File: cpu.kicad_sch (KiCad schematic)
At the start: 30 parts, among them J81 Conn_01x03_Pin, J82 Conn_Coaxial, J83 Conn_Coaxial, J84 Conn_01x02_Pin, SW81 SW_Push, SW82 SW_Push, U8 ESP32-C6-MINI-1U, U81 74HC595, U82 74HC595, U83 74HC595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

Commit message: Scan deleted.
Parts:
- removed C90: 0u1, Capacitor_SMD:C_0402_1005Metric, symbol Device:C
- removed U83: 74HC595, Package_SO:SOIC-16_3.9x9.9mm_P1.27mm, symbol 74xx:74HC595
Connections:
- net MonA0: now also U82.3 (QD)
- net MonA1: now also U82.2 (QC)
- net MonB0: now also U82.1 (QB)
- net MonB1: now also U82.15 (QA)
- net OffsetA0: no longer U82.7 (QH)
- net OffsetA1: no longer U82.6 (QG)
- net OffsetA2: no longer U82.5 (QF)
- net SHSel: no longer U82.4 (QE)
- net Sel1A: now also U82.7 (QH)
- net Sel1B: now also U82.6 (QG)
- net Sel2A: now also U82.5 (QF)
- net Sel2B: now also U82.4 (QE)
- net SHHoldG1: no longer names the net of U81.4 (QE)
- net SHHoldG2: no longer names the net of U81.15 (QA)
- net SHOutEn1: no longer names the net of U81.7 (QH)
- net SHOutEn2: no longer names the net of U81.3 (QD)
- net SHSample1: no longer names the net of U81.6 (QG)
- net SHSample2: no longer names the net of U81.2 (QC)
- net SHSampleG1: no longer names the net of U81.5 (QF)
- net SHSampleG2: no longer names the net of U81.1 (QB)
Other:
- moved on the sheet: C87, C88, C89, R87, U81, U82

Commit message: Most blocks there....
About to restore scan.
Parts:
- R83: footprint Resistor_SMD:R_0603_1608Metric -> Resistor_SMD:R_0402_1005Metric; LCSC C23140 -> C25105
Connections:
- net OffsetA0: now also U81.7 (QH)
- net OffsetA1: now also U81.6 (QG)
- net OffsetA2: now also U81.5 (QF)
- net SHSel: now also U81.4 (QE)
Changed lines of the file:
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@@
 	)
 	(no_connect
-		(at 119.38 107.95)
+		(at 118.11 107.95)
 	)
 	(no_connect
@@
 	)
 	(no_connect
-		(at 119.38 113.03)
+		(at 118.11 113.03)
 	)
 	(no_connect
@@
 	)
 	(no_connect
-		(at 119.38 105.41)
+		(at 118.11 105.41)
 	)
 	(no_connect
@@
 	)
 	(no_connect
-		(at 119.38 110.49)
+		(at 118.11 110.49)
 	)
 	(no_connect
@@
 	(wire
 		(pts
-			(xy 119.38 123.19) (xy 120.65 123.19)
-		)
-		(stroke
-			(width 0)
-			(type default)
-		)
-	)
-	(wire
-		(pts
-			(xy 119.38 118.11) (xy 120.65 118.11)
-		)
-		(stroke
-			(width 0)
-			(type default)
-		)
-	)
-	(wire
-		(pts
 			(xy 170.18 115.57) (xy 171.45 115.57)
 		)
@@
 	(wire
 		(pts
-			(xy 119.38 115.57) (xy 120.65 115.57)
-		)
-		(stroke
-			(width 0)
-			(type default)
-		)
-	)
-	(wire
-		(pts
 			(xy 57.15 48.26) (xy 80.01 48.26)
 		)
@@
 	(wire
 		(pts
-			(xy 119.38 120.65) (xy 120.65 120.65)
-		)
-		(stroke
-			(width 0)
-			(type default)
-		)
-	)
-	(wire
-		(pts
 			(xy 71.12 71.12) (xy 80.01 71.12)
 		)
@@
 	(hierarchical_label "OffsetA0"
 		(shape output)
-		(at 120.65 123.19 0)
+		(at 118.11 123.19 0)
 		(effects
 			(font
@@
 	(hierarchical_label "SHSel"
 		(shape output)
-		(at 120.65 115.57 0)
+		(at 118.11 115.57 0)
 		(effects
 			(font
@@
 	(hierarchical_label "OffsetA2"
 		(shape output)
-		(at 120.65 118.11 0)
+		(at 118.11 118.11 0)
 		(effects
 			(font
@@
 	(hierarchical_label "OffsetA1"
 		(shape output)
-		(at 120.65 120.65 0)
+		(at 118.11 120.65 0)
 		(effects
 			(font
@@
 	)
 	(symbol
-		(lib_name "Conn_Coaxial_1")
 		(lib_id "Connector:Conn_Coaxial")
 		(at 190.5 62.23 0)
@@
 			)
 		)
-		(property "Footprint" "Resistor_SMD:R_0603_1608Metric"
+		(property "Footprint" "Resistor_SMD:R_0402_1005Metric"
 			(at 175.26 60.452 90)
 			(effects
@@
 			)
 		)
-		(property "LCSC" "C23140"
+		(property "LCSC" "C25105"
 			(at 175.26 62.23 90)
 			(effects

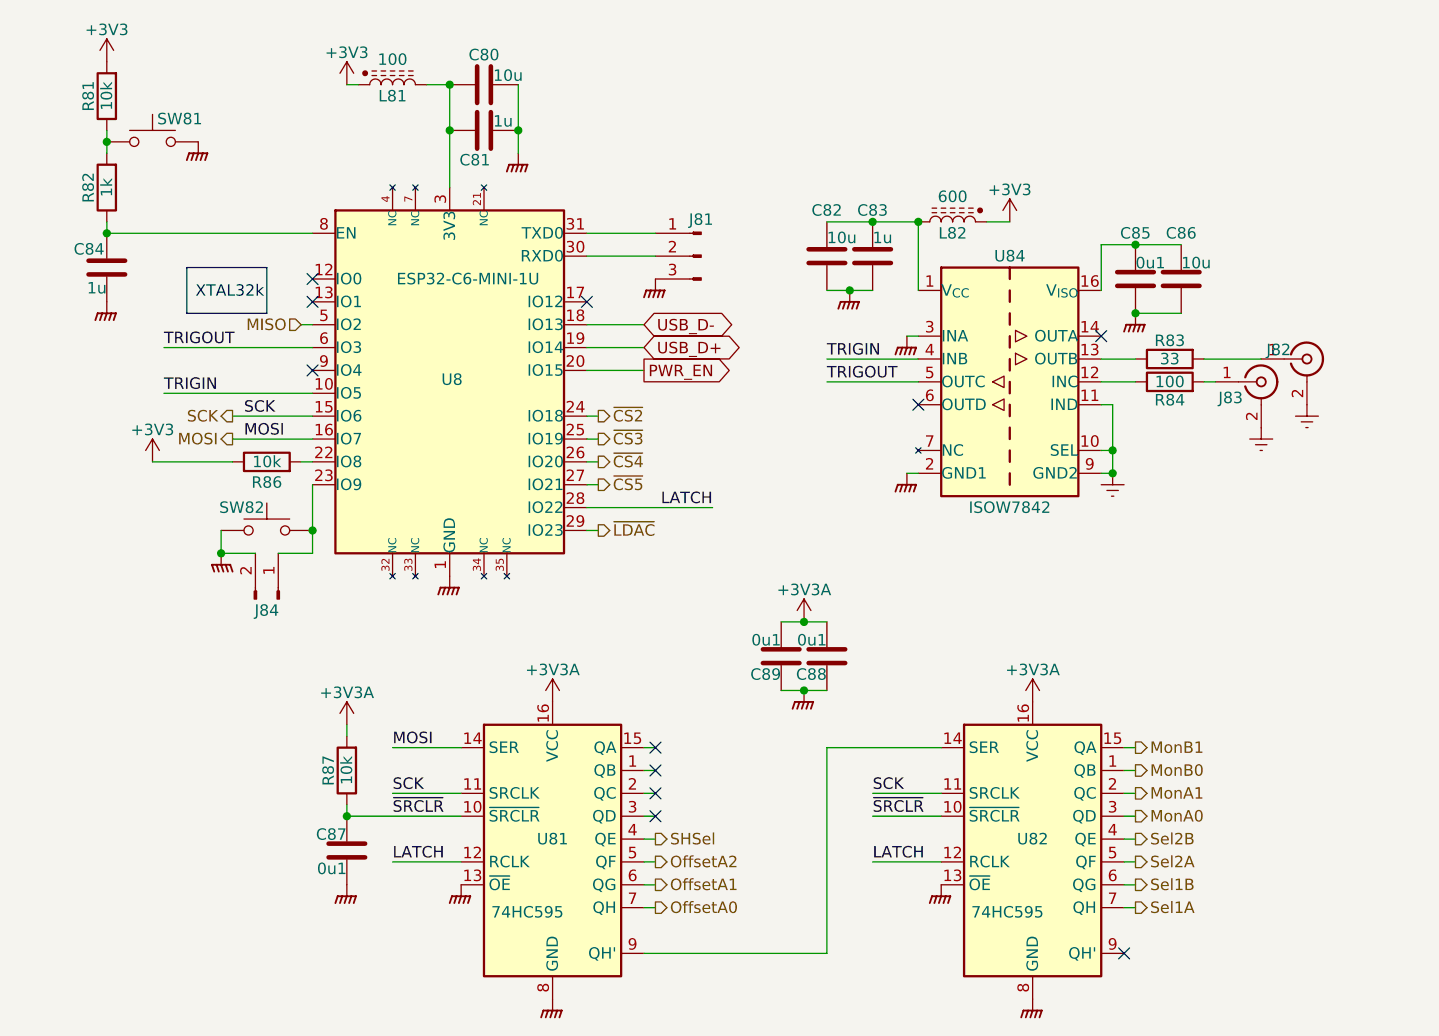
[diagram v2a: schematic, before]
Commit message: Put ref filtering into the schematic.
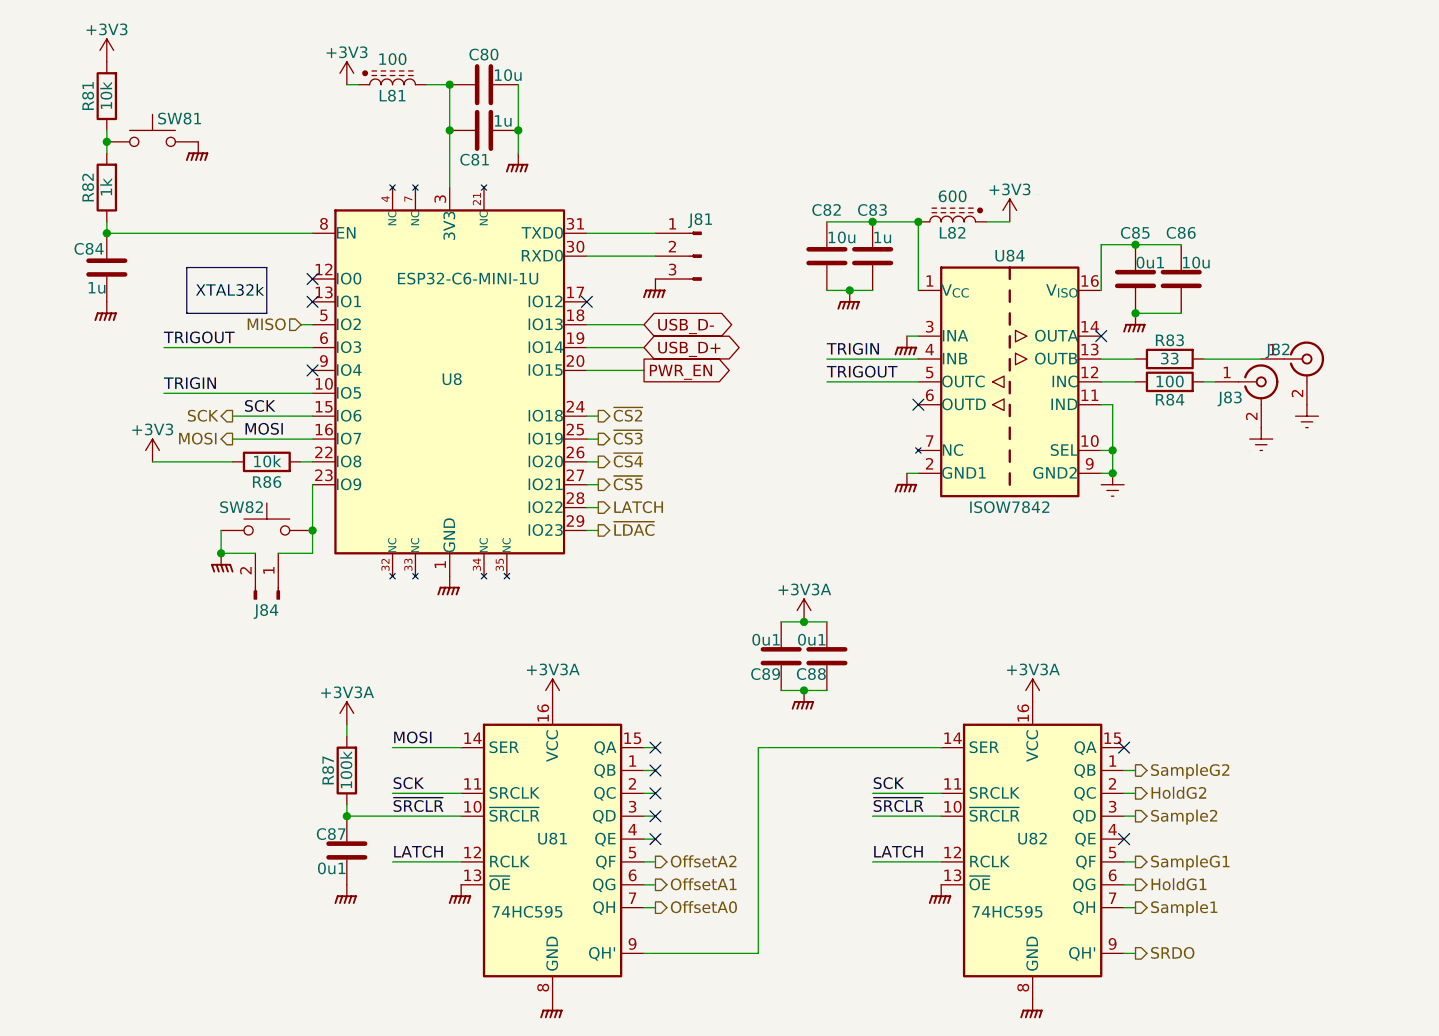
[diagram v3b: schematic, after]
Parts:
- R87: value 10k -> 100k; LCSC C25744 -> (none)
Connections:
- net SRDO: now reaches U82.9 (QH')
- net MonA0 renamed Sample2
- net MonA1 renamed HoldG2
- net MonB0 renamed SampleG2
- net MonB1: no longer names the net of U82.15 (QA)
- net SHSel: no longer names the net of U81.4 (QE)
- net Sel1A renamed Sample1
- net Sel1B renamed HoldG1
- net Sel2A renamed SampleG1
- net Sel2B: no longer names the net of U82.4 (QE)
- no-connect marks 11 -> 13
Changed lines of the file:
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@@
 	)
 	(no_connect
+		(at 170.18 105.41)
+	)
+	(no_connect
+		(at 118.11 115.57)
+	)
+	(no_connect
 		(at 118.11 113.03)
 	)
 	(no_connect
-		(at 80.01 53.34)
+		(at 170.18 115.57)
 	)
 	(no_connect
-		(at 118.11 105.41)
+		(at 80.01 53.34)
 	)
 	(no_connect
-		(at 170.18 128.27)
+		(at 118.11 105.41)
 	)
 	(no_connect
@@
 	(wire
 		(pts
-			(xy 170.18 105.41) (xy 171.45 105.41)
+			(xy 76.2 83.82) (xy 80.01 83.82)
 		)
 		(stroke
@@
 	(wire
 		(pts
-			(xy 76.2 83.82) (xy 80.01 83.82)
+			(xy 129.54 105.41) (xy 149.86 105.41)
 		)
 		(stroke
@@
 	(wire
 		(pts
-			(xy 137.16 105.41) (xy 149.86 105.41)
+			(xy 146.05 59.69) (xy 147.32 59.69)
 		)
 		(stroke
@@
 	(wire
 		(pts
-			(xy 146.05 59.69) (xy 147.32 59.69)
+			(xy 170.18 113.03) (xy 171.45 113.03)
 		)
 		(stroke
@@
 	(wire
 		(pts
-			(xy 137.16 128.27) (xy 116.84 128.27)
+			(xy 129.54 128.27) (xy 116.84 128.27)
 		)
 		(stroke
@@
 	(wire
 		(pts
-			(xy 171.45 49.53) (xy 176.53 49.53)
+			(xy 170.18 107.95) (xy 171.45 107.95)
 		)
 		(stroke
@@
 	(wire
 		(pts
-			(xy 170.18 113.03) (xy 171.45 113.03)
+			(xy 170.18 110.49) (xy 171.45 110.49)
 		)
 		(stroke
@@
 	(wire
 		(pts
-			(xy 83.82 102.87) (xy 83.82 104.14)
+			(xy 171.45 49.53) (xy 176.53 49.53)
 		)
 		(stroke
@@
 	(wire
 		(pts
-			(xy 88.9 110.49) (xy 96.52 110.49)
+			(xy 83.82 102.87) (xy 83.82 104.14)
 		)
 		(stroke
@@
 	(wire
 		(pts
-			(xy 170.18 115.57) (xy 171.45 115.57)
+			(xy 88.9 110.49) (xy 96.52 110.49)
 		)
 		(stroke
@@
 	(wire
 		(pts
-			(xy 110.49 78.74) (xy 124.46 78.74)
+			(xy 110.49 78.74) (xy 111.76 78.74)
 		)
 		(stroke
@@
 	(wire
 		(pts
-			(xy 146.05 74.93) (xy 147.32 74.93)
+			(xy 170.18 128.27) (xy 171.45 128.27)
 		)
 		(stroke
@@
 	(wire
 		(pts
-			(xy 167.64 49.53) (xy 171.45 49.53)
+			(xy 146.05 74.93) (xy 147.32 74.93)
 		)
 		(stroke
@@
 	(wire
 		(pts
-			(xy 179.07 64.77) (xy 180.34 64.77)
+			(xy 167.64 49.53) (xy 171.45 49.53)
 		)
 		(stroke
@@
 	(wire
 		(pts
-			(xy 78.74 73.66) (xy 80.01 73.66)
+			(xy 179.07 64.77) (xy 180.34 64.77)
 		)
 		(stroke
@@
 	(wire
 		(pts
-			(xy 170.18 107.95) (xy 171.45 107.95)
+			(xy 78.74 73.66) (xy 80.01 73.66)
 		)
 		(stroke
@@
 	(wire
 		(pts
-			(xy 137.16 128.27) (xy 137.16 105.41)
+			(xy 129.54 128.27) (xy 129.54 105.41)
 		)
 		(stroke
@@
 	(wire
 		(pts
-			(xy 170.18 110.49) (xy 171.45 110.49)
-		)
-		(stroke
-			(width 0)
-			(type default)
-		)
-	)
-	(wire
-		(pts
 			(xy 83.82 111.76) (xy 83.82 113.03)
 		)
@@
 		)
 	)
-	(label "LATCH"
-		(at 124.46 78.74 180)
-		(effects
-			(font
-				(size 1.27 1.27)
-			)
-			(justify right bottom)
-		)
-	)
 	(label "SCK"
 		(at 72.39 68.58 0)
@@
 		)
 	)
-	(hierarchical_label "MonA1"
+	(hierarchical_label "HoldG2"
 		(shape output)
 		(at 171.45 110.49 0)
@@
 		)
 	)
-	(hierarchical_label "Sel2B"
+	(hierarchical_label "Sample2"
 		(shape output)
-		(at 171.45 115.57 0)
+		(at 171.45 113.03 0)
 		(effects
 			(font
@@
 		)
 	)
-	(hierarchical_label "Sel1B"
+	(hierarchical_label "SampleG1"
 		(shape output)
-		(at 171.45 120.65 0)
+		(at 171.45 118.11 0)
 		(effects
 			(font
@@
 		)
 	)
-	(hierarchical_label "SHSel"
+	(hierarchical_label "~{LDAC}"
 		(shape output)
-		(at 118.11 115.57 0)
+		(at 111.76 81.28 0)
 		(effects
 			(font
@@
 		)
 	)
-	(hierarchical_label "~{LDAC}"
+	(hierarchical_label "OffsetA2"
 		(shape output)
-		(at 111.76 81.28 0)
+		(at 118.11 118.11 0)
 		(effects
 			(font
@@
 		)
 	)
-	(hierarchical_label "OffsetA2"
+	(hierarchical_label "~{CS3}"
 		(shape output)
-		(at 118.11 118.11 0)
+		(at 111.76 71.12 0)
 		(effects
 			(font
@@
 		)
 	)
-	(hierarchical_label "MonB1"
+	(hierarchical_label "SRDO"
 		(shape output)
-		(at 171.45 105.41 0)
+		(at 171.45 128.27 0)
 		(effects
 			(font
@@
 		)
 	)
-	(hierarchical_label "MonB0"
+	(hierarchical_label "LATCH"
 		(shape output)
-		(at 171.45 107.95 0)
+		(at 111.76 78.74 0)
 		(effects
 			(font
@@
 		)
 	)
-	(hierarchical_label "~{CS3}"
+	(hierarchical_label "SampleG2"
 		(shape output)
-		(at 111.76 71.12 0)
+		(at 171.45 107.95 0)
 		(effects
 			(font
@@
 		)
 	)
-	(hierarchical_label "Sel1A"
+	(hierarchical_label "Sample1"
 		(shape output)
 		(at 171.45 123.19 0)
@@
 		)
 	)
-	(hierarchical_label "Sel2A"
+	(hierarchical_label "HoldG1"
 		(shape output)
-		(at 171.45 118.11 0)
+		(at 171.45 120.65 0)
 		(effects
 			(font
@@
 		)
 	)
-	(hierarchical_label "MonA0"
-		(shape output)
-		(at 171.45 113.03 0)
-		(effects
-			(font
-				(size 1.27 1.27)
-			)
-			(justify left)
-		)
-	)
 	(hierarchical_label "OffsetA1"
 		(shape output)
@@
 			)
 		)
-		(property "Value" "10k"
+		(property "Value" "100k"
 			(at 83.82 107.95 90)
 			(effects
@@
 			)
 		)
-		(property "LCSC" "C25744"
+		(property "LCSC" ""
 			(at 83.82 107.95 90)
 			(effects

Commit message: Progress checkin.  About to redo FDA feedback again.
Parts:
- renumbered R87 to R85
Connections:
- net +3V3: now also R81.1; no longer R81.2
- net +3V3A: now also R85.1, U81.10 (~{SRCLR}); no longer R85.2
- net ~{SRCLR}: now also R85.2; no longer R85.1, U81.10 (~{SRCLR})
- net at C84.1, U8.8 (EN): now also R82.2; no longer R82.1
- new net: R81.2, R82.1, SW81.1
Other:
- moved on the sheet: C87, C88, C89, R81, R82, R85

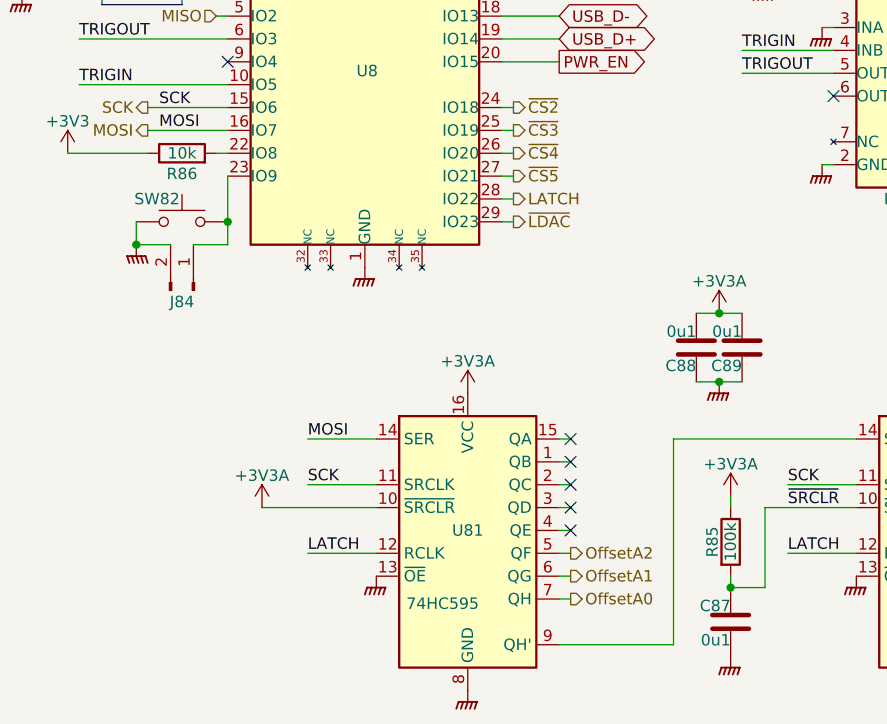
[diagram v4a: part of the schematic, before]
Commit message: Start to place within physical board size.
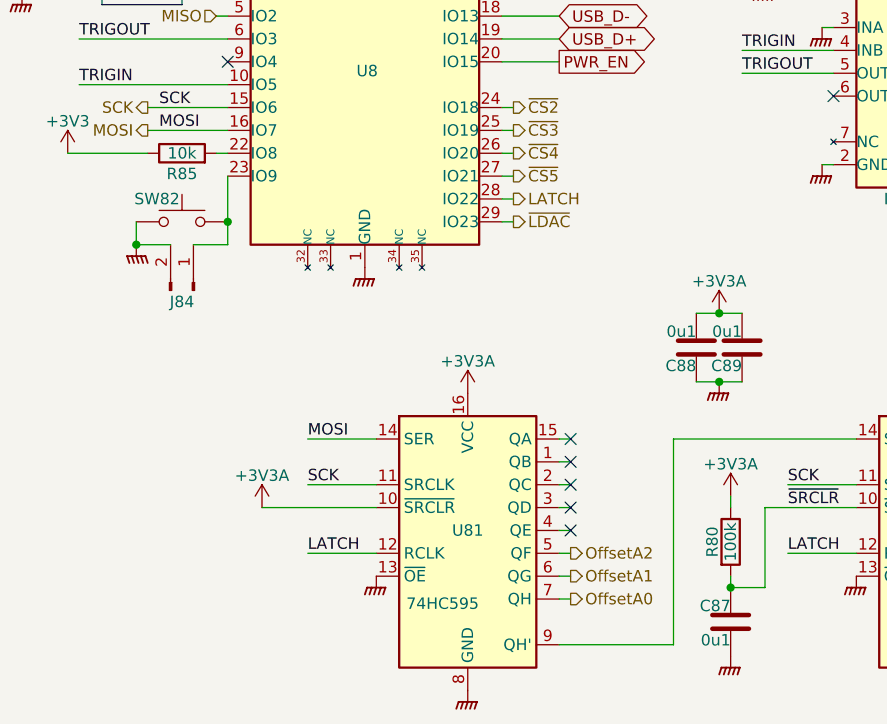
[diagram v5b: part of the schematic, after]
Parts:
- U8: footprint RF_Module:ESP32-C6-MINI-1 -> Parts:ESP32-C6-MINI-1U
- renumbered R85 to R80, R86 to R85
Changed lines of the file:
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@@
 		(on_board yes)
 		(dnp no)
-		(property "Reference" "R86"
+		(property "Reference" "R85"
 			(at 74.93 75.946 90)
 			(effects
@@
 			(project "lincal"
 				(path "/b054cef4-39e3-49d8-aff0-7ba5a206c187/5e75b7d0-06d7-44d3-9715-75151d16c7a9"
-					(reference "R86")
+					(reference "R85")
 					(unit 1)
 				)
@@
 		(on_board yes)
 		(dnp no)
-		(property "Reference" "R85"
+		(property "Reference" "R80"
 			(at 133.858 116.84 90)
 			(effects
@@
 			(project "lincal"
 				(path "/b054cef4-39e3-49d8-aff0-7ba5a206c187/5e75b7d0-06d7-44d3-9715-75151d16c7a9"
-					(reference "R85")
+					(reference "R80")
 					(unit 1)
 				)
@@
 			)
 		)
-		(property "Footprint" "RF_Module:ESP32-C6-MINI-1"
+		(property "Footprint" "Parts:ESP32-C6-MINI-1U"
 			(at 95.25 64.77 0)
 			(do_not_autoplace yes)

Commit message: Adjust placements
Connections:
- net Earth: now also C85.2, C86.2
- net GNDPWR: no longer C85.2, C86.2
- net CPU_EN: now reaches C84.1, R82.2, U8.8 (EN)
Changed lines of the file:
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@@
 	)
 	(junction
+		(at 171.45 57.15)
+		(diameter 0)
+		(color 0 0 0 0)
+	)
+	(junction
 		(at 135.89 121.92)
 		(diameter 0)
@@
 	)
 	(junction
-		(at 171.45 57.15)
-		(diameter 0)
-		(color 0 0 0 0)
-	)
-	(junction
 		(at 171.45 49.53)
 		(diameter 0)
@@
 		)
 	)
+	(label "CPU_EN"
+		(at 59.69 48.26 0)
+		(effects
+			(font
+				(size 1.27 1.27)
+			)
+			(justify left bottom)
+		)
+	)
 	(label "TRIGOUT"
 		(at 137.16 64.77 0)
@@
 	)
 	(symbol
+		(lib_id "power:Earth")
+		(at 171.45 57.15 0)
+		(unit 1)
+		(exclude_from_sim no)
+		(in_bom yes)
+		(on_board yes)
+		(dnp no)
+		(property "Reference" "#PWR086"
+			(at 171.45 63.5 0)
+			(effects
+				(font
+					(size 1.27 1.27)
+				)
+				(hide yes)
+			)
+		)
+		(property "Value" "Earth"
+			(at 171.45 60.96 0)
+			(effects
+				(font
+					(size 1.27 1.27)
+				)
+				(hide yes)
+			)
+		)
+		(property "Footprint" ""
+			(at 171.45 57.15 0)
+			(effects
+				(font
+					(size 1.27 1.27)
+				)
+				(hide yes)
+			)
+		)
+		(property "Datasheet" "~"
+			(at 171.45 57.15 0)
+			(effects
+				(font
+					(size 1.27 1.27)
+				)
+				(hide yes)
+			)
+		)
+		(property "Description" "Power symbol creates a global label with name \"Earth\""
+			(at 171.45 57.15 0)
+			(effects
+				(font
+					(size 1.27 1.27)
+				)
+				(hide yes)
+			)
+		)
+		(pin "1"
+		)
+		(instances
+			(project "lincal"
+				(path "/b054cef4-39e3-49d8-aff0-7ba5a206c187/5e75b7d0-06d7-44d3-9715-75151d16c7a9"
+					(reference "#PWR086")
+					(unit 1)
+				)
+			)
+		)
+	)
+	(symbol
 		(lib_id "power:GNDPWR")
 		(at 57.15 55.88 0)
@@
 					(unit 1)
 				)
-			)
-		)
-	)
-	(symbol
-		(lib_id "power:GNDPWR")
-		(at 171.45 57.15 0)
-		(unit 1)
-		(exclude_from_sim no)
-		(in_bom yes)
-		(on_board yes)
-		(dnp no)
-		(property "Reference" "#PWR0708"
-			(at 171.45 63.5 0)
-			(effects
-				(font
-					(size 1.27 1.27)
-				)
-				(hide yes)
-			)
-		)
-		(property "Value" "GNDPWR"
-			(at 171.45 60.452 0)
-			(effects
-				(font
-					(size 1.27 1.27)
-				)
-				(hide yes)
-			)
-		)
-		(property "Footprint" ""
-			(at 171.45 58.42 0)
-			(effects
-				(font
-					(size 1.27 1.27)
-				)
-				(hide yes)
-			)
-		)
-		(property "Datasheet" "~"
-			(at 171.45 58.42 0)
-			(effects
-				(font
-					(size 1.27 1.27)
-				)
-				(hide yes)
-			)
-		)
-		(property "Description" "Power symbol creates a global label with name \"GNDPWR\" , global ground"
-			(at 171.45 57.15 0)
-			(effects
-				(font
-					(size 1.27 1.27)
-				)
-				(hide yes)
-			)
-		)
-		(pin "1"
-		)
-		(instances
-			(project "lincal"
-				(path "/b054cef4-39e3-49d8-aff0-7ba5a206c187/5e75b7d0-06d7-44d3-9715-75151d16c7a9"
-					(reference "#PWR0708")
-					(unit 1)
-				)
